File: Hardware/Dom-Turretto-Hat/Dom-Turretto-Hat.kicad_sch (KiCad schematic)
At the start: 10 parts

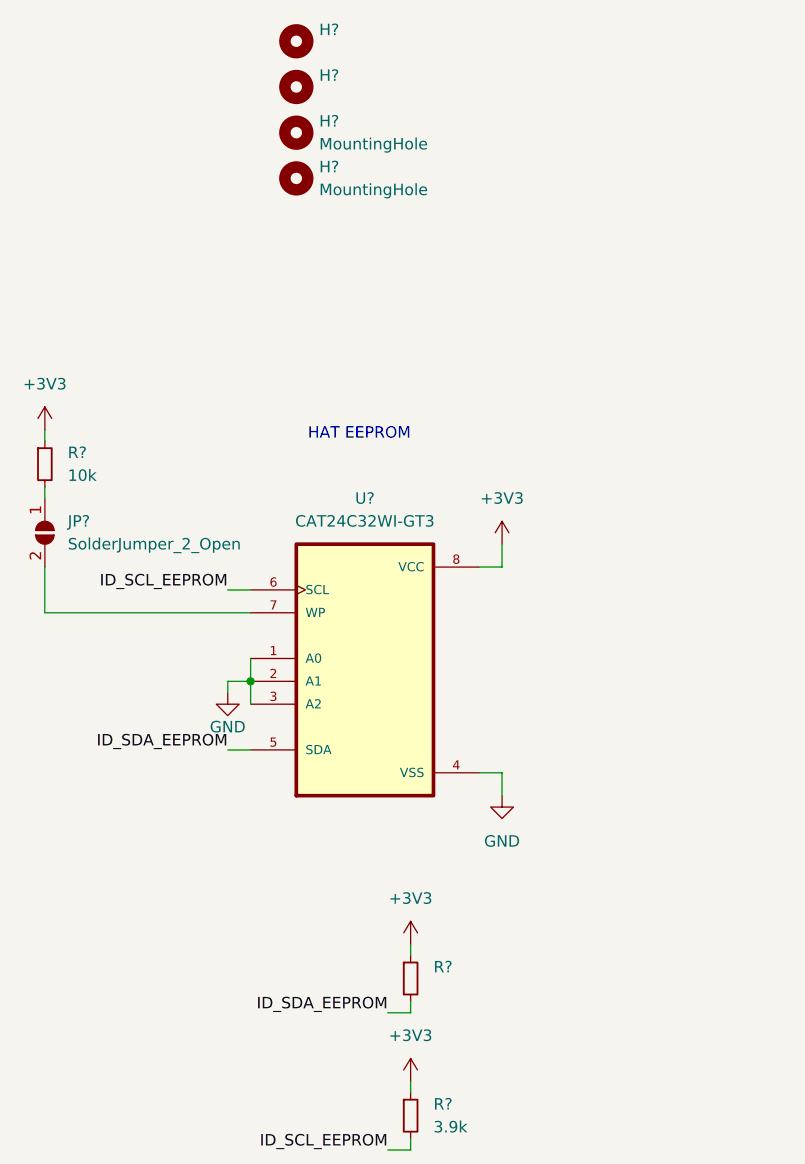
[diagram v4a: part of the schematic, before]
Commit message: Add buck converter
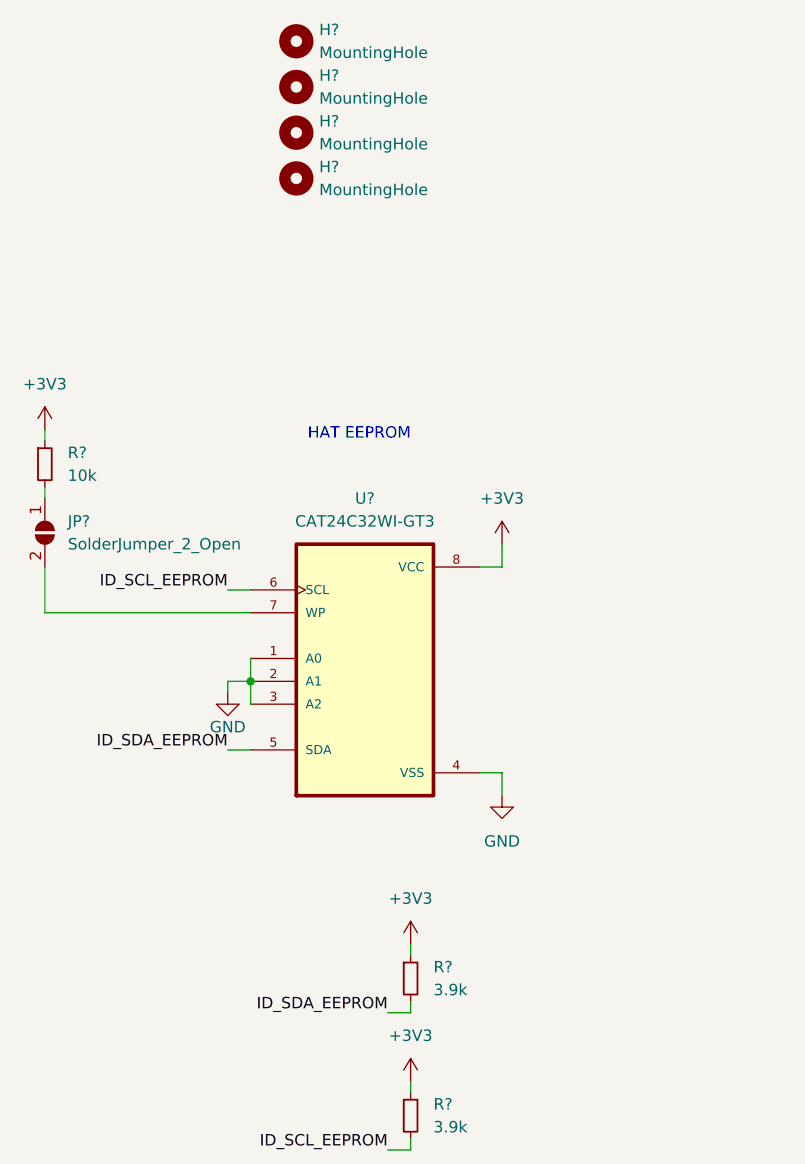
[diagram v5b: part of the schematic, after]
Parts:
- H? (x2): value (none) -> MountingHole
- R?: value (none) -> 3.9k
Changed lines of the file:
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@@
       (effects (font (size 1.27 1.27)) (justify right))
     )
-    (property "Value" "" (id 1) (at 59.69 35.5599 90)
+    (property "Value" "MountingHole" (id 1) (at 59.69 35.5599 90)
       (effects (font (size 1.27 1.27)) (justify right))
     )
@@
       (effects (font (size 1.27 1.27)) (justify left))
     )
-    (property "Value" "" (id 1) (at 59.69 40.6399 0)
+    (property "Value" "MountingHole" (id 1) (at 59.69 40.6399 0)
       (effects (font (size 1.27 1.27)) (justify left))
     )
@@
       (effects (font (size 1.27 1.27)) (justify left))
     )
-    (property "Value" "" (id 1) (at 72.39 139.6999 0)
+    (property "Value" "3.9k" (id 1) (at 72.39 139.6999 0)
       (effects (font (size 1.27 1.27)) (justify left))
     )
@@
       (reference "#PWR?") (unit 1) (value "+3V3") (footprint "")
     )
-    (path "/12e93b0c-a239-457f-b141-0c3b73a9b90a/017e27ba-0db7-4d28-9040-f5496f011e69"
-      (reference "#PWR?") (unit 1) (value "VCC") (footprint "")
-    )
     (path "/28fd1fbc-026b-4dd2-b303-4aef81adb474/020c7563-050d-4993-a33e-5454a0d9355c"
       (reference "#PWR?") (unit 1) (value "+3V3") (footprint "")
@@
       (reference "#PWR?") (unit 1) (value "VCC") (footprint "")
     )
-    (path "/12e93b0c-a239-457f-b141-0c3b73a9b90a/16740cdb-7f52-4447-94ab-740d0f478995"
-      (reference "#PWR?") (unit 1) (value "GND") (footprint "")
-    )
-    (path "/12e93b0c-a239-457f-b141-0c3b73a9b90a/16b178c0-cc95-4427-addb-6062f60cd08c"
-      (reference "#PWR?") (unit 1) (value "GND") (footprint "")
-    )
     (path "/12e93b0c-a239-457f-b141-0c3b73a9b90a/1b25e470-d0bf-46dc-a169-527bd3e96bab"
       (reference "#PWR?") (unit 1) (value "GND") (footprint "")
     )
-    (path "/12e93b0c-a239-457f-b141-0c3b73a9b90a/1efd17b6-e056-4c7c-bc96-f053cd9192c3"
-      (reference "#PWR?") (unit 1) (value "GND") (footprint "")
-    )
     (path "/12e93b0c-a239-457f-b141-0c3b73a9b90a/23a39806-5bcf-46b3-9dd9-56270df61814"
       (reference "#PWR?") (unit 1) (value "GND") (footprint "")
     )
+    (path "/12e93b0c-a239-457f-b141-0c3b73a9b90a/2493902d-ffa7-493e-8f09-d359ed621591"
+      (reference "#PWR?") (unit 1) (value "GND") (footprint "")
+    )
     (path "/12e93b0c-a239-457f-b141-0c3b73a9b90a/279b3b38-0ca0-4170-b0e5-b4a71141ec1d"
       (reference "#PWR?") (unit 1) (value "VCC") (footprint "")
@@
       (reference "#PWR?") (unit 1) (value "GND") (footprint "")
     )
+    (path "/12e93b0c-a239-457f-b141-0c3b73a9b90a/462f3a13-0050-4845-84df-8be913b4f9b0"
+      (reference "#PWR?") (unit 1) (value "VCC") (footprint "")
+    )
     (path "/28fd1fbc-026b-4dd2-b303-4aef81adb474/46550aaa-c0b4-4d92-bd6b-7e22e8b199b7"
       (reference "#PWR?") (unit 1) (value "+3V3") (footprint "")
@@
       (reference "#PWR?") (unit 1) (value "GND") (footprint "")
     )
+    (path "/12e93b0c-a239-457f-b141-0c3b73a9b90a/4ae1d417-485a-437f-8fe9-cf7ad21c0f01"
+      (reference "#PWR?") (unit 1) (value "GND") (footprint "")
+    )
     (path "/12e93b0c-a239-457f-b141-0c3b73a9b90a/4c1f75b9-e0c3-44e8-a481-a723b8533cb1"
       (reference "#PWR?") (unit 1) (value "GND") (footprint "")
     )
     (path "/28fd1fbc-026b-4dd2-b303-4aef81adb474/52af071e-05f3-4b5a-bd70-eb8982ac5712"
-      (reference "#PWR?") (unit 1) (value "VCC") (footprint "")
-    )
-    (path "/12e93b0c-a239-457f-b141-0c3b73a9b90a/530e57de-d399-4db4-8ce9-5d03e3f39020"
       (reference "#PWR?") (unit 1) (value "VCC") (footprint "")
     )
@@
       (reference "#PWR?") (unit 1) (value "~") (footprint "")
     )
+    (path "/12e93b0c-a239-457f-b141-0c3b73a9b90a/65aa81f2-00ad-4ff8-9c97-6233eef1878e"
+      (reference "#PWR?") (unit 1) (value "+5V") (footprint "")
+    )
     (path "/12e93b0c-a239-457f-b141-0c3b73a9b90a/6768a302-0668-48df-aa2b-97708aad38b6"
       (reference "#PWR?") (unit 1) (value "GND") (footprint "")
@@
       (reference "#PWR?") (unit 1) (value "GND") (footprint "")
     )
+    (path "/12e93b0c-a239-457f-b141-0c3b73a9b90a/ef21a8b1-2228-4fe0-8e53-070fce64f3d9"
+      (reference "#PWR?") (unit 1) (value "GND") (footprint "")
+    )
     (path "/f85fb8de-9851-4c0e-b74d-825a175d5ab1"
       (reference "#PWR?") (unit 1) (value "+3V3") (footprint "")
+    )
+    (path "/12e93b0c-a239-457f-b141-0c3b73a9b90a/fb96ab52-d7dd-42f6-bfd5-b842696d789c"
+      (reference "#PWR?") (unit 1) (value "GND") (footprint "")
     )
     (path "/28fd1fbc-026b-4dd2-b303-4aef81adb474/fc935fe0-8219-452b-9c6c-b59c1b60386d"
@@
       (reference "A?") (unit 1) (value "Pololu_Breakout_A4988") (footprint "Module:Pololu_Breakout-16_15.2x20.3mm")
     )
-    (path "/12e93b0c-a239-457f-b141-0c3b73a9b90a/0538551b-9562-47ef-ba34-68c9ff71a548"
-      (reference "C?") (unit 1) (value "10uF") (footprint "")
-    )
     (path "/28fd1fbc-026b-4dd2-b303-4aef81adb474/0d2126d3-7c5a-4f8d-8c25-4c5c18a46630"
       (reference "C?") (unit 1) (value "47uF") (footprint "")
     )
+    (path "/12e93b0c-a239-457f-b141-0c3b73a9b90a/190a6eba-f018-4f03-b257-e6db43cb1c7b"
+      (reference "C?") (unit 1) (value "10nF") (footprint "")
+    )
     (path "/12e93b0c-a239-457f-b141-0c3b73a9b90a/1e3bdcbd-8bf4-4d5f-8901-dadb4d9ff406"
       (reference "C?") (unit 1) (value "1uF") (footprint "Capacitor_SMD:C_0603_1608Metric")
@@
       (reference "C?") (unit 1) (value "10uF") (footprint "Capacitor_SMD:C_0603_1608Metric")
     )
-    (path "/12e93b0c-a239-457f-b141-0c3b73a9b90a/35bf006d-decb-4cf1-b6dd-099f97f69adf"
-      (reference "C?") (unit 1) (value "10uF") (footprint "")
-    )
     (path "/12e93b0c-a239-457f-b141-0c3b73a9b90a/4882251c-5e11-49eb-857a-7faa3ac6183c"
       (reference "C?") (unit 1) (value "0.1uF") (footprint "")
@@
       (reference "C?") (unit 1) (value "10uF") (footprint "Capacitor_SMD:C_0603_1608Metric")
     )
+    (path "/12e93b0c-a239-457f-b141-0c3b73a9b90a/70060f5d-b007-495f-a45f-7f1bfc4b8949"
+      (reference "C?") (unit 1) (value "180uF") (footprint "")
+    )
+    (path "/12e93b0c-a239-457f-b141-0c3b73a9b90a/881129b8-1053-44b9-bbe7-c43d6d8c66c3"
+      (reference "C?") (unit 1) (value "6.8uF") (footprint "")
+    )
     (path "/12e93b0c-a239-457f-b141-0c3b73a9b90a/a1caa1de-048f-4c18-adf1-b4bfaebe3c4b"
       (reference "C?") (unit 1) (value "4.7uF") (footprint "Capacitor_SMD:C_0603_1608Metric")
     )
+    (path "/12e93b0c-a239-457f-b141-0c3b73a9b90a/ba2d8e02-8dff-41f2-94ab-2977ba7494f7"
+      (reference "C?") (unit 1) (value "6.8uF") (footprint "")
+    )
     (path "/12e93b0c-a239-457f-b141-0c3b73a9b90a/ebe526ad-ca36-421c-84ae-0ce5a8516f08"
       (reference "C?") (unit 1) (value "100nF") (footprint "Capacitor_SMD:C_0603_1608Metric")
     )
+    (path "/12e93b0c-a239-457f-b141-0c3b73a9b90a/ec276c8a-eb48-440f-b539-492777d28831"
+      (reference "C?") (unit 1) (value "22uF") (footprint "")
+    )
     (path "/12e93b0c-a239-457f-b141-0c3b73a9b90a/f545c142-5d8e-40c4-b0fe-7c045a9cac0e"
       (reference "C?") (unit 1) (value "0.1uF") (footprint "")
     )
+    (path "/12e93b0c-a239-457f-b141-0c3b73a9b90a/8a6cabaa-212f-4145-a004-b1da07d438ec"
+      (reference "D?") (unit 1) (value "D_Schottky") (footprint "")
+    )
+    (path "/12e93b0c-a239-457f-b141-0c3b73a9b90a/20d61a98-9d76-48c3-aea7-5d687e7dcd59"
+      (reference "EXT_POW") (unit 1) (value "LED") (footprint "")
+    )
     (path "/1a3a61a0-89d4-4ac0-9b09-269e6ad8da57"
       (reference "H?") (unit 1) (value "MountingHole") (footprint "")
@@
       (reference "JP?") (unit 1) (value "SolderJumper_2_Open") (footprint "")
     )
+    (path "/12e93b0c-a239-457f-b141-0c3b73a9b90a/89b193d6-28e4-4647-a3aa-6b8779163e05"
+      (reference "L?") (unit 1) (value "29uH") (footprint "")
+    )
     (path "/c8c14f7c-55ef-44f2-9b65-a499409017e1/d6c763e2-1952-4281-9868-501fafa3b154"
       (reference "L?") (unit 1) (value "27nH") (footprint "Inductor_SMD:L_0603_1608Metric")
     )
+    (path "/12e93b0c-a239-457f-b141-0c3b73a9b90a/53065c22-5d58-4a1d-924c-019ba026a13b"
+      (reference "PI_POW") (unit 1) (value "LED") (footprint "")
+    )
     (path "/2b40ab8c-3e2e-41fa-8219-59ccff88db81"
       (reference "R?") (unit 1) (value "3.9k") (footprint "")
@@
       (reference "R?") (unit 1) (value "10k") (footprint "")
     )
+    (path "/12e93b0c-a239-457f-b141-0c3b73a9b90a/e93d172e-4818-4231-a3ae-739f87af7028"
+      (reference "R?") (unit 1) (value "1k") (footprint "")
+    )
+    (path "/12e93b0c-a239-457f-b141-0c3b73a9b90a/fdd22b43-7b45-4042-a6f9-6eedcac49126"
+      (reference "R?") (unit 1) (value "1k") (footprint "")
+    )
     (path "/28fd1fbc-026b-4dd2-b303-4aef81adb474/302cb40a-2337-4eb6-a685-7b9f8bf14844"
       (reference "R_Opt?") (unit 1) (value "10k") (footprint "")
@@
       (reference "Stepper?") (unit 1) (value "Conn_01x04_Male") (footprint "")
     )
-    (path "/12e93b0c-a239-457f-b141-0c3b73a9b90a/1784dc37-b4b5-445e-bcf0-620781e628fa"
-      (reference "U?") (unit 1) (value "LM1085-5.0") (footprint "")
+    (path "/12e93b0c-a239-457f-b141-0c3b73a9b90a/07f473c2-dbb9-400c-8bca-062c33fea70b"
+      (reference "U?") (unit 1) (value "LM22679TJ-5.0{slash}NOPB") (footprint "TO127P1401X200-7N")
     )
     (path "/2502caee-d955-453d-8eae-fa5e480fab5f"

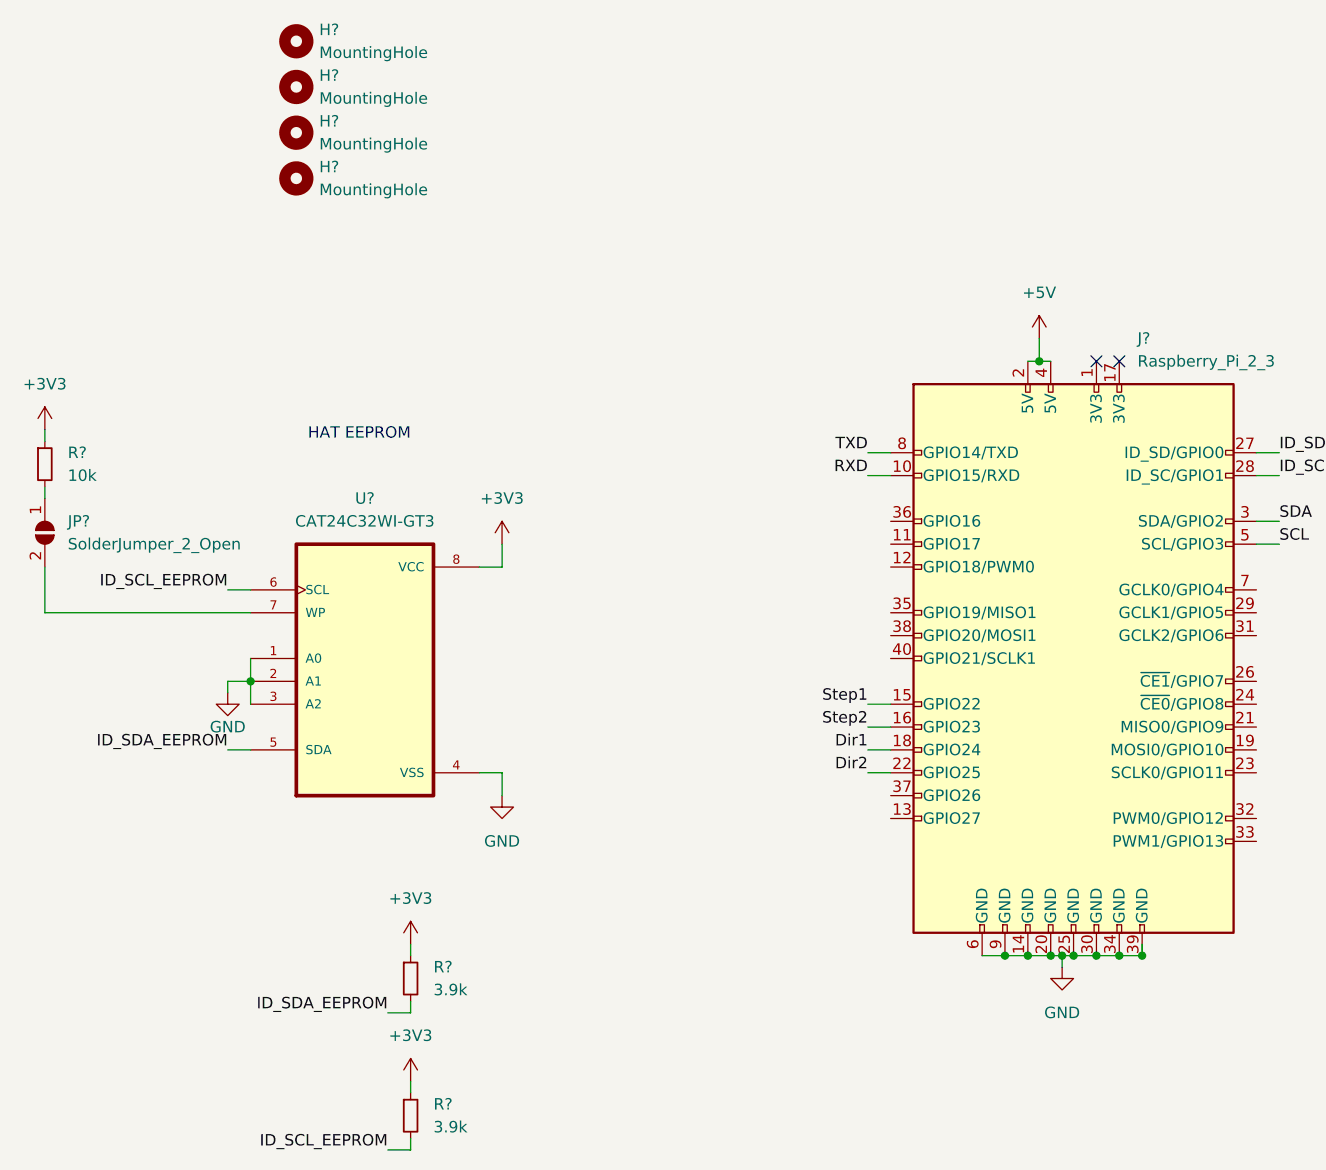
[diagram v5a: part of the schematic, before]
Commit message: Assigned footprints
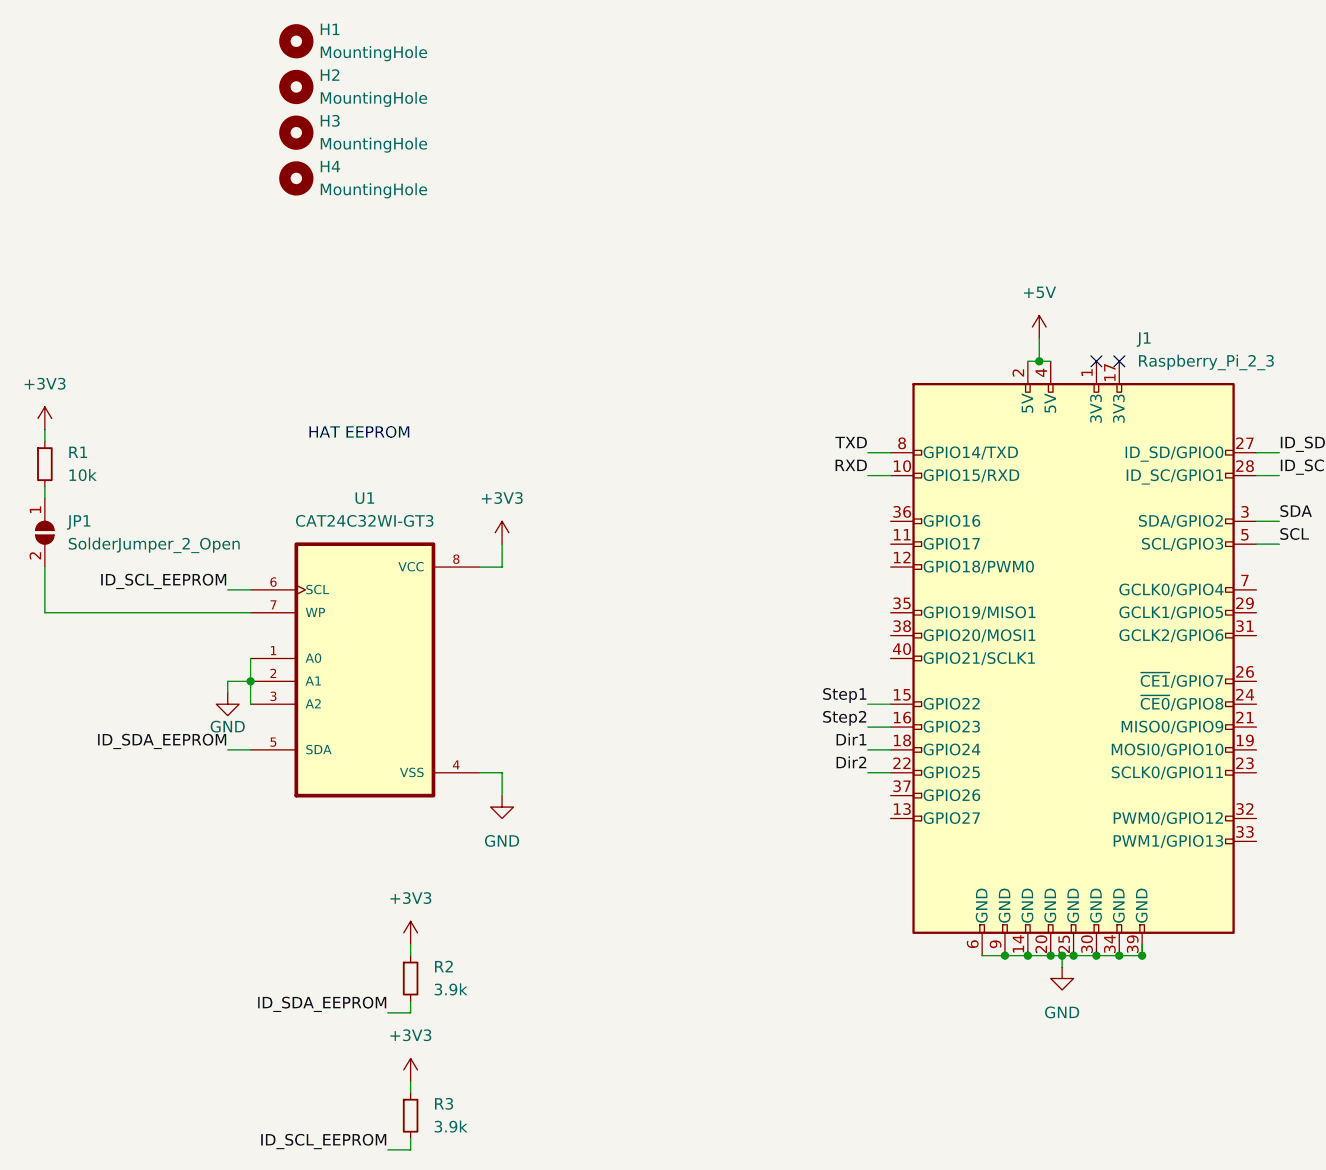
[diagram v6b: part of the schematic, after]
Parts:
- U1: renamed from U?; footprint SOIC127P600X175-8N -> (none)
- gave numbers to parts that had none: 9
